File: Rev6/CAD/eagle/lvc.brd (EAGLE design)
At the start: 31.8 x 31.8 mm, 31 parts, among them J1 3,5MM_1X2_SCREWTERM, J2 3,5MM_1X2_SCREWTERM, Q1 SI7997DP, U1 L78L33ACUTR, U2 TLV170IDBVR

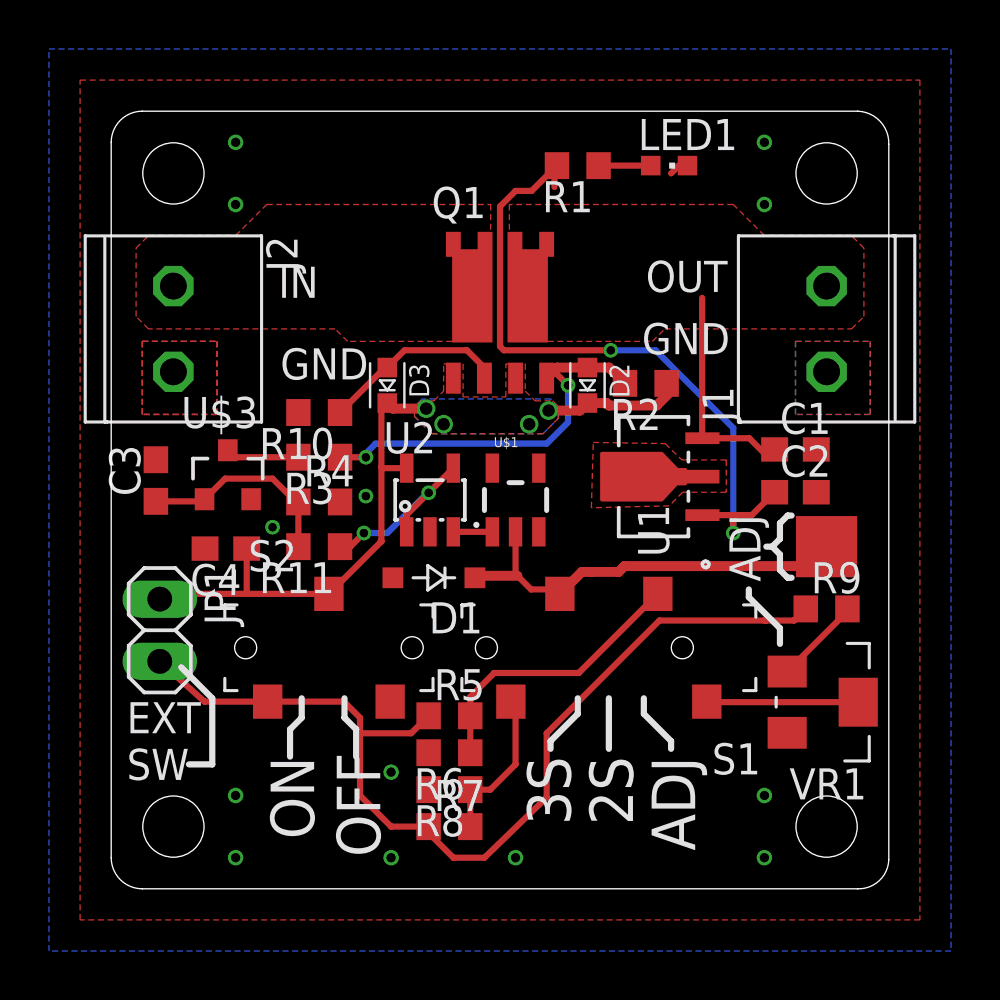
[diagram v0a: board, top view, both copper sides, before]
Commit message: Updated buffer to be upstream of comparator
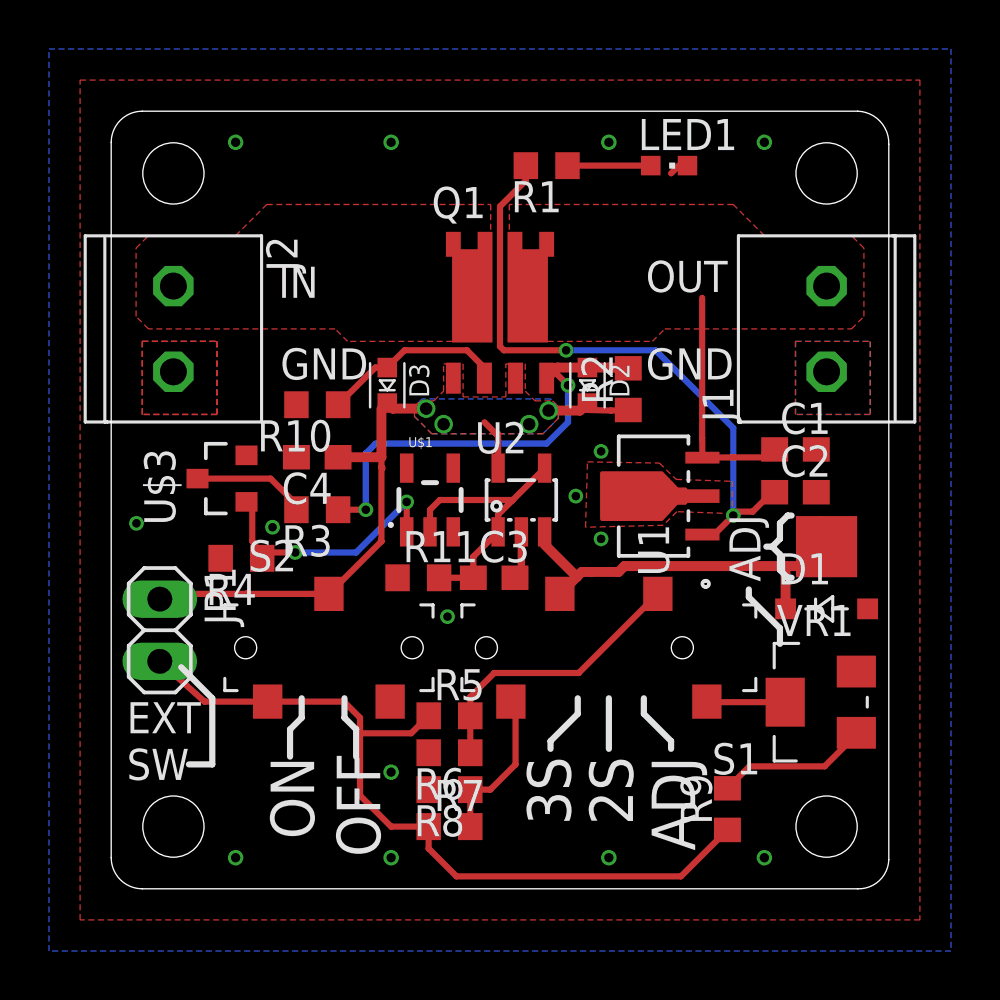
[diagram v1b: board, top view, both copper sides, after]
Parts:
- C3: value 0.33uF -> 50pF
- R11: value 3k -> 100k; device resistor:R0603 -> rcl:R0603
- moved D1 16.1 mm to (29.2, 11.4), turned to 0 degrees
- moved C3 14.4 mm to (15.6, 12.7), turned to 0 degrees
- moved R9 9.12 mm to (25.2, 3.25), turned to 90 degrees
- moved C4 5.28 mm to (8.41, 17.6)
- moved R11 4.24 mm to (12.5, 12.7), turned to 0 degrees
- moved R4 3.92 mm to (5.32, 13.5), turned to 180 degrees
- moved U2 3.73 mm to (16.7, 15.9)
- moved U$1 3.49 mm to (13.0, 15.9)
- moved R3 2.14 mm to (8.41, 15.5)
- moved R1 1.27 mm to (17.8, 29.5)
- moved U1 0.79 mm to (22.1, 16.0)
- moved R2 0.75 mm to (21.1, 20.4), turned to 90 degrees
- moved R10 0.33 mm to (8.41, 19.8)
- moved U$3 0.29 mm to (4.52, 16.7), turned to 90 degrees
- moved VR1 0.08 mm to (29.0, 7.62), turned to 0 degrees
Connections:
- removed net CUTOFF: U$1.1, U2.3
- removed net N$1: R11.1, U2.1, U2.4
- new net V_DIV_BUF: C3.1, R11.2, U$1.2, U2.1, U2.4
- net GND: now also R11.1
- net LOAD: now also U$1.1; no longer C3.1, R11.2
- net V_DIV: now also U2.3; no longer U$1.2
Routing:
- net V_DIV_BUF: track 0.00 -> 11.5 mm
- net N$1: track 7.94 -> 0.00 mm, vias 2 -> 0
- net EN: track 40.5 -> 33.3 mm
- net N$8: track 6.19 -> 3.21 mm
- net N$11: track 3.58 -> 6.24 mm
- net LED: track 28.9 -> 26.3 mm
- net LOAD: track 8.42 -> 10.6 mm, vias 0 -> 2
- net N$5: track 16.1 -> 18.1 mm
- net N$7: track 3.00 -> 4.69 mm
- net GND: track 0.80 -> 2.42 mm, vias 13 -> 15
- net CUTOFF: track 1.59 -> 0.00 mm
- net V_DIV: track 18.4 -> 16.9 mm
- net N$4: track 2.13 -> 3.40 mm
- net VOUT: track 9.01 -> 9.99 mm
- net V+: track 26.1 -> 25.2 mm

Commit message: Updated diode footprints
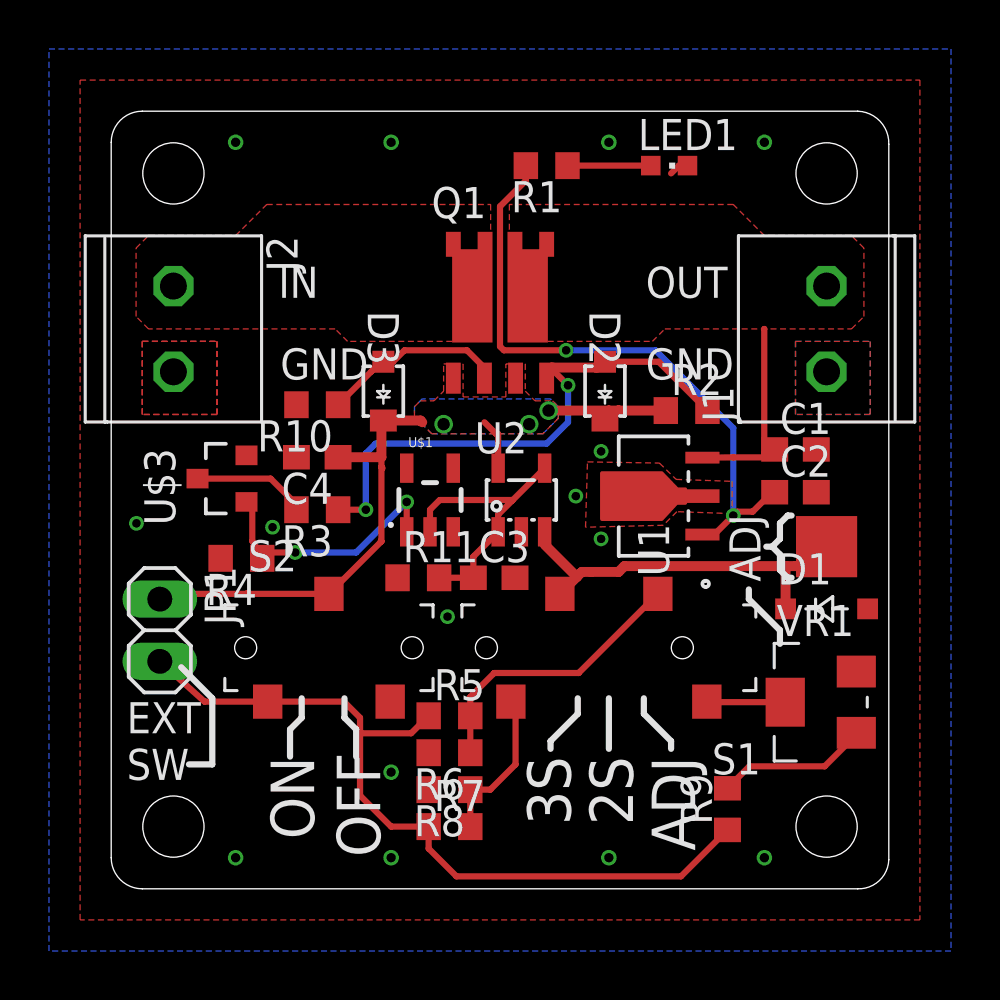
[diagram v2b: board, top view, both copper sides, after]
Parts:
- removed TP1: TESTPOINT, CM_test:TP_2.5MM
- added TP2: TESTPOINTNOCREAM, CM_test:TP_2.5MM_NOCREAM
- C3: value 50pF -> 47pF
- D2, D3: value MM3Z12VC -> DZ2J120M0L; device NR_diode:SOD-323F -> LR_zener:SMINI2-F5-B
- moved R2 2.54 mm to (23.5, 19.5), turned to 0 degrees
- moved D2 0.75 mm to (20.2, 20.3)
- moved D3 0.29 mm to (11.1, 20.3)
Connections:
- net N$5: now also D2.A; no longer D2.1
- net N$6: now also D3.A; no longer D3.1
- net V+: now also D2.C, D3.C; no longer D2.2, D3.2
- net V_DIV: now also TP2.P$1; no longer TP1.P$1
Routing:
- net N$5: track 18.1 -> 22.5 mm
- net VOUT: track 9.99 -> 8.71 mm
- net V+: track 25.2 -> 26.4 mm, vias 4 -> 3
- net GND: track 2.42 -> 1.41 mm
- net V_DIV: track 16.9 -> 16.3 mm

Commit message: Cleaned up component naming on Rev 1
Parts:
- removed U$1: NCP300LSN33T1G, onsemi:SOT23-5
- added U3: TLV170IDBVR, LR_op_amps:SOT23-DBV
- U1: value L78L33ACUTR -> NCP300LSN33T1G; device LR_vreg:SOT-89 -> onsemi:SOT23-5
- U2: value TLV170IDBVR -> L78L33ACUTR; device LR_op_amps:SOT23-DBV -> LR_vreg:SOT-89
- moved U1 9.13 mm to (13.0, 15.9), turned to 0 degrees
- moved U2 5.40 mm to (22.1, 16.0), turned to 90 degrees
- renumbered U$3 to Q2
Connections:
- net GND: now also U1.3, U3.2; no longer U$1.3, U1.2
- net LED: now also U2.1; no longer U1.1
- net LOAD: now also U1.1; no longer U$1.1
- net V+: now also U3.5; no longer U2.5
- net VOUT: now also U2.3; no longer U1.3
- net V_DIV: now also U3.3; no longer U2.3
- net V_DIV_BUF: now also U1.2, U3.1, U3.4; no longer U$1.2, U2.1, U2.4
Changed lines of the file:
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@@
 <element name="R10" library="resistor" library_urn="urn:adsk.eagle:library:348" package="R0603" package3d_urn="urn:adsk.eagle:package:26057/1" value="1M" x="8.41375" y="19.764375" rot="R180"/>
 <element name="Q1" library="AR_transistor" package="POWERPAK-SO-8-DUAL" value="SI7997DP" x="15.875" y="23.574375"/>
-<element name="U$1" library="onsemi" package="SOT23-5" value="NCP300LSN33T1G" x="13.0175" y="15.875"/>
-<element name="U$3" library="rohm1" package="SOT23" value="RR7002BMT116" x="4.524375" y="16.748125" rot="R90"/>
+<element name="U1" library="onsemi" package="SOT23-5" value="NCP300LSN33T1G" x="13.0175" y="15.875"/>
+<element name="Q2" library="rohm1" package="SOT23" value="RR7002BMT116" x="4.524375" y="16.748125" rot="R90"/>
 <element name="C2" library="rcl" library_urn="urn:adsk.eagle:library:334" package="C0603" package3d_urn="urn:adsk.eagle:package:23616/2" value="0.1uF" x="27.94" y="16.1925">
 <attribute name="SPICEPREFIX" value="C" x="27.94" y="16.1925" size="1.778" layer="27" display="off"/>
@@
 </element>
 <element name="D1" library="vishay1" package="SOD123" value="BZT52B8V2" x="29.21" y="11.43"/>
-<element name="U1" library="LR_vreg" package="SOT-89" value="L78L33ACUTR" x="22.145625" y="16.03375" rot="R90">
+<element name="U2" library="LR_vreg" package="SOT-89" value="L78L33ACUTR" x="22.145625" y="16.03375" rot="R90">
 <attribute name="MANUFACTURER_PART_NUMBER" value="L78L33ACUTR" x="22.145625" y="16.03375" size="1.778" layer="27" rot="R90" display="off"/>
 <attribute name="VENDOR" value="STMicroelectronics" x="22.145625" y="16.03375" size="1.778" layer="27" rot="R90" display="off"/>
 </element>
-<element name="U2" library="LR_op_amps" package="SOT23-DBV" value="TLV170IDBVR" x="16.748125" y="15.875"/>
+<element name="U3" library="LR_op_amps" package="SOT23-DBV" value="TLV170IDBVR" x="16.748125" y="15.875"/>
 <element name="C4" library="rcl" library_urn="urn:adsk.eagle:library:334" package="C0603" package3d_urn="urn:adsk.eagle:package:23616/2" value="0.1uF" x="8.41375" y="17.62125" rot="R180">
 <attribute name="SPICEPREFIX" value="C" x="8.41375" y="17.62125" size="1.778" layer="27" rot="R180" display="off"/>
@@
 <via x="20.32" y="1.27" extent="1-16" drill="0.381"/>
 <contactref element="R10" pad="2"/>
-<contactref element="U$1" pad="3"/>
+<contactref element="U1" pad="3"/>
 <via x="11.43" y="4.7625" extent="1-16" drill="0.381"/>
-<contactref element="U$3" pad="2"/>
+<contactref element="Q2" pad="2"/>
 <contactref element="C1" pad="2"/>
 <contactref element="C2" pad="2"/>
@@
 <contactref element="D1" pad="A"/>
 <via x="5.08" y="1.27" extent="1-16" drill="0.381"/>
-<contactref element="U1" pad="2"/>
+<contactref element="U2" pad="2"/>
 <polygon width="0.254" layer="1" thermals="no" rank="3">
 <vertex x="4.318" y="19.3675"/>
@@
 <vertex x="30.988" y="22.352"/>
 </polygon>
-<contactref element="U2" pad="2"/>
+<contactref element="U3" pad="2"/>
 <contactref element="C4" pad="2"/>
 <wire x1="23.530625" y1="29.5275" x2="23.1775" y2="29.5275" width="0.254" layer="1"/>
@@
 <wire x1="5.55625" y1="12.0425" x2="3.073125" y2="12.0425" width="0.254" layer="1"/>
 <wire x1="3.073125" y1="12.0425" x2="1.984375" y2="11.826875" width="0.254" layer="1"/>
-<contactref element="U2" pad="5"/>
+<contactref element="U3" pad="5"/>
 <contactref element="C4" pad="1"/>
 <wire x1="8.89" y1="12.0425" x2="11.033125" y2="14.185625" width="0.254" layer="1"/>
@@
 <signal name="LOAD">
 <contactref element="R4" pad="1"/>
-<contactref element="U$3" pad="1"/>
-<contactref element="U$1" pad="1"/>
+<contactref element="Q2" pad="1"/>
+<contactref element="U1" pad="1"/>
 <via x="7.51485" y="13.731875" extent="1-16" drill="0.35"/>
 <via x="12.065" y="15.795625" extent="1-16" drill="0.35"/>
@@
 <signal name="N$7">
 <contactref element="R3" pad="2"/>
-<contactref element="U$3" pad="3"/>
+<contactref element="Q2" pad="3"/>
 <wire x1="3.524375" y1="16.748125" x2="6.50875" y2="16.748125" width="0.254" layer="1"/>
 <wire x1="6.50875" y1="16.748125" x2="7.56375" y2="15.693125" width="0.254" layer="1"/>
@@
 <contactref element="Q1" pad="5L"/>
 <contactref element="C1" pad="1"/>
-<contactref element="U1" pad="3"/>
+<contactref element="U2" pad="3"/>
 <polygon width="0.254" layer="1" thermals="no">
 <vertex x="30.734" y="26.162"/>
@@
 <wire x1="19.5975" y1="12.94625" x2="19.605625" y2="12.938125" width="0.254" layer="1"/>
 <wire x1="20.955" y1="13.17625" x2="27.543125" y2="13.17625" width="0.4064" layer="1"/>
-<contactref element="U2" pad="3"/>
+<contactref element="U3" pad="3"/>
 <wire x1="27.543125" y1="13.17625" x2="27.94" y2="13.17625" width="0.4064" layer="1"/>
 <wire x1="27.94" y1="13.17625" x2="28.41625" y2="13.17625" width="0.4064" layer="1"/>
@@
 <contactref element="C2" pad="1"/>
 <contactref element="R1" pad="2"/>
-<contactref element="U1" pad="1"/>
+<contactref element="U2" pad="1"/>
 <wire x1="16.93" y1="29.5275" x2="17.168125" y2="29.765625" width="0.254" layer="1"/>
 <wire x1="15.875" y1="22.145625" x2="16.03375" y2="21.986875" width="0.254" layer="1"/>
@@
 </signal>
 <signal name="V_DIV_BUF">
-<contactref element="U$1" pad="2"/>
-<contactref element="U2" pad="1"/>
-<contactref element="U2" pad="4"/>
+<contactref element="U1" pad="2"/>
+<contactref element="U3" pad="1"/>
+<contactref element="U3" pad="4"/>
 <wire x1="17.698125" y1="17.175" x2="16.3746875" y2="15.8515625" width="0.254" layer="1"/>
 <wire x1="16.3746875" y1="15.8515625" x2="15.798125" y2="15.275" width="0.254" layer="1"/>
